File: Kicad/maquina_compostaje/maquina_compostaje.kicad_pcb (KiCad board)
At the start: 2 copper layers, 97 parts, among them J1 Conn_01x06, J2 Conn_01x09, J3 Conn_01x04, J4 Conn_01x04, J5 Conn_01x03, J6 Barrel_Jack_MountingPin, J7 Conn_01x06, J8 Conn_01x04, Q1 BC328, Q2 BC328, Q3 BC328, Q4 BC328, Q5 BC328, Q6 BC328, Q7 BC328, Q8 BC328, SW1 1825910-6, SW2 1825910-6, U1 ESP32-WROOM-32, U2 TLP281-4GB(F), U3 TLP281-4GB(F), U4 L298N, U5 L298N, U6 AMS1117-5.0, U7 AMS1117-3.3, U8 LM393, U9 A3144

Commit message: inicio del ruteo
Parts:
- added C17: 0.1uF, Capacitor_SMD:C_1206_3216Metric_Pad1.33x1.80mm_HandSolder, F.Cu at (96.4, 71.6)
- added C18: 10uF, Capacitor_SMD:C_1206_3216Metric_Pad1.33x1.80mm_HandSolder, F.Cu at (93.5, 71.6)
- added R33: 4.7K, Resistor_SMD:R_1206_3216Metric_Pad1.30x1.75mm_HandSolder, F.Cu at (120.4, 150.3)
- added R34: 4.7K, Resistor_SMD:R_1206_3216Metric_Pad1.30x1.75mm_HandSolder, F.Cu at (123.3, 150.2)
- added R35: 4.7K, Resistor_SMD:R_1206_3216Metric_Pad1.30x1.75mm_HandSolder, F.Cu at (92.1, 80.4)
- added R36: 4.7K, Resistor_SMD:R_1206_3216Metric_Pad1.30x1.75mm_HandSolder, F.Cu at (96.1, 76.5)
- D1, D10, D11, D12, D13, D14, D15, D16, D2, D3, D4, D5, D6, D7, D8, D9: footprint M7:DIOM505270X240 -> Diode_SMD:D_SOD-128
- D17: footprint Diode_THT:D_DO-41_SOD81_P10.16mm_Horizontal -> Diode_SMD:D_SOD-128
- J2: value Conn_01x09 -> Conenctor_GPIO; footprint Connector_JST:JST_EH_B9B-EH-A_1x09_P2.50mm_Vertical -> Connector_JST:JST_EH_B5B-EH-A_1x05_P2.50mm_Vertical
- Q1, Q2, Q3, Q4, Q5, Q6, Q7, Q8: footprint Package_TO_SOT_THT:TO-92_Inline -> Package_TO_SOT_SMD:SOT-23
- R2, R3: value 470 -> 4.7K
- SW1: value 1825910-6 -> RESET; footprint 1825910-6:SW_1825910-6-4 -> w_switch:smd_push2
- SW2: value 1825910-6 -> BOOT; footprint 1825910-6:SW_1825910-6-4 -> w_switch:smd_push2
- U2, U3: footprint TLP281-4GB_F_:SOIC127P700X210-16N -> Package_SO:SO-16_5.3x10.2mm_P1.27mm
- U6: footprint AMS1117-5:SOT229P700X180-4N -> Package_TO_SOT_SMD:SOT-223
- U7: footprint AMS1117-3:SOT229P700X180-4N -> Package_TO_SOT_SMD:SOT-223
- moved J8 94.7 mm to (153.6, 108.2), turned to 90 degrees
- moved J4 88.4 mm to (153.8, 137.1), turned to 90 degrees
- moved R20 78.7 mm to (72.4, 95.3), turned to -90 degrees
- moved R22 76.6 mm to (63.2, 110.5), turned to 90 degrees
- moved C3 71.3 mm to (84.3, 83.8)
- moved R23 69.0 mm to (70.6, 117.9), turned to 90 degrees
- moved R21 67.4 mm to (66.4, 114.7), turned to 90 degrees
- moved R25 67.3 mm to (83.9, 114.8), turned to 90 degrees
- moved C5 65.5 mm to (130.7, 98.5)
- moved R18 62.5 mm to (80.0, 95.3), turned to -90 degrees
- moved R19 61.3 mm to (76.2, 95.3), turned to -90 degrees
- moved Q7 60.7 mm to (76.5, 111.8), turned to 180 degrees
- moved Q6 59.0 mm to (71.6, 111.8), turned to 180 degrees
- moved J7 58.4 mm to (132.8, 152.4), turned to 0 degrees
- moved R28 56.8 mm to (88.2, 111.8), turned to 90 degrees
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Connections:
- net /ESP32/Hall_sensor renamed Hall_sensor
- net /ESP32/M_A1 renamed M_A1
- net /ESP32/M_A2 renamed M_A2
- net /ESP32/M_A3 renamed M_A3
- net /ESP32/M_A4 renamed M_A4
- net /ESP32/M_B1 renamed M_B1
- net /ESP32/M_B2 renamed M_B2
- net /ESP32/M_B3 renamed M_B3
- net /ESP32/M_B4 renamed M_B4
- net /ESP32/Touch_sensor renamed Touch_sensor
- net /Power supply/bypass 3.3v renamed 3.3V
- C10 pad 1: /Power supply/bypass 5v -> 5V
- C11 pad 1: /Power supply/bypass 5v -> 5V
- C12 pad 2: unconnected-(C12-Pad2) -> GND
- C3 pad 1: /Motor A/5V -> 5V
- C4 pad 1: /Motor A/12V -> 12V
- C5 pad 1: /Motor B/5V -> 5V
- C6 pad 1: /Motor A/12V -> 12V
- C8 pad 1: /Power supply/bypass 5v -> 5V
- C9 pad 1: /Power supply/bypass 5v -> 5V
- D18 pad 2: /Power supply/bypass 5v -> 5V
- D19 pad 2: /Power supply/bypass 5v -> 5V
- F2 pad 2: /Motor A/12V -> 12V
- J2 pad 2: /ESP32/gpio4 -> /ESP32/gpio16
- J2 pad 3: /ESP32/gpio5 -> /ESP32/gpio17
- J2 pad 4: /ESP32/gpio16 -> /ESP32/gpio23
- J2 pad 5: /ESP32/gpio17 -> /ESP32/gpio35
- J5 pad 1: /Power supply/bypass 5v -> 5V
- J7 pad 2: /ESP32/RX -> RX
- J7 pad 3: /ESP32/TX -> TX
- J7 pad 4: /Power supply/bypass 5v -> 5V
- J8 pad 1: /ESP32/SDA -> SDA
- J8 pad 2: /ESP32/SCL -> SCL
- Q5 pad 1: GND -> /Motor B/IN 4B
- Q6 pad 1: GND -> /Motor B/IN 3B
- Q7 pad 1: GND -> /Motor B/IN 2B
- R10 pad 1: /Motor A/12V -> 12V
- R11 pad 1: /Motor A/12V -> 12V
- R12 pad 1: /Motor A/12V -> 12V
- R13 pad 1: /Motor A/12V -> 12V
- R14 pad 1: /Motor A/12V -> 12V
- R15 pad 1: /Motor A/12V -> 12V
- R16 pad 1: /Motor A/12V -> 12V
- R2 pad 1: Net-(R2-Pad1) -> SCL
- R2 pad 2: /ESP32/RX -> +3.3V
- R21 pad 1: /Motor A/12V -> 12V
- R22 pad 1: /Motor A/12V -> 12V
- R22 pad 2: GND -> /Motor B/IN 4B
- R23 pad 1: /Motor A/12V -> 12V
- R24 pad 1: /Motor A/12V -> 12V
- R24 pad 2: GND -> /Motor B/IN 3B
- R25 pad 1: /Motor A/12V -> 12V
- R26 pad 1: /Motor A/12V -> 12V
- R26 pad 2: GND -> /Motor B/IN 2B
- R27 pad 1: /Motor A/12V -> 12V
- R28 pad 1: /Motor A/12V -> 12V
- R3 pad 1: Net-(R3-Pad1) -> SDA
- R3 pad 2: /ESP32/TX -> +3.3V
- R30 pad 1: /Power supply/bypass 5v -> 5V
- R32 pad 1: /Power supply/bypass 5v -> 5V
- R9 pad 1: /Motor A/12V -> 12V
- RV1 pad 1: +5V -> 5V
- U1 pad 26: /ESP32/gpio4 -> EN_1A
- U1 pad 29: /ESP32/gpio5 -> EN_2A
- U1 pad 33: /ESP32/SDA -> SDA
- U1 pad 34: Net-(R3-Pad1) -> TX
- U1 pad 35: Net-(R2-Pad1) -> RX
- U1 pad 36: /ESP32/SCL -> SCL
- U1 pad 6: /ESP32/gpio34 -> EN_2B
- U1 pad 9: /ESP32/gpio33 -> EN_1B
- U4 pad 11: /Motor A/EN B -> EN_2A
- U4 pad 4: /Motor A/12V -> 12V
- U4 pad 6: /Motor A/EN A -> EN_1A
- U4 pad 9: /Motor A/5V -> 5V
- U5 pad 10: GND -> /Motor B/IN 3B
- U5 pad 11: /Motor B/EN_2B -> EN_2B
- U5 pad 12: GND -> /Motor B/IN 4B
- U5 pad 4: /Motor A/12V -> 12V
- U5 pad 6: /Motor B/EN_1B -> EN_1B
- U5 pad 7: GND -> /Motor B/IN 2B
- U5 pad 9: /Motor B/5V -> 5V
- U6 pad 2: /Power supply/bypass 5v -> 5V
- U7 pad 3: /Power supply/bypass 5v -> 5V
- U8 pad 8: /Power supply/bypass 5v -> 5V
- U9 pad 1: /Power supply/bypass 5v -> 5V
- U9 pad 2: Net-(C16-Pad1) -> GND
- U9 pad 3: unconnected-(U9-Pad3) -> Net-(C16-Pad1)
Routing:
- net GND: track 0.00 -> 451.7 mm, vias 0 -> 12
- net 12V: track 0.00 -> 149.9 mm
- net 5V: track 0.00 -> 133.6 mm, vias 0 -> 2
- net /Motor B/IN 3B: track 0.00 -> 65.9 mm, vias 0 -> 1
- net /Motor A/IN 3A: track 0.00 -> 59.7 mm, vias 0 -> 1
- net /Motor B/IN 2B: track 0.00 -> 57.4 mm, vias 0 -> 1
- net /Motor B/IN 4B: track 0.00 -> 56.3 mm, vias 0 -> 1
- net /Motor A/IN 2A: track 0.00 -> 51.7 mm, vias 0 -> 1
- net 3.3V: track 0.00 -> 50.7 mm
- net /Motor A/IN 4A: track 0.00 -> 50.6 mm, vias 0 -> 1
- net /Motor B/OUT 1: track 0.00 -> 48.8 mm
- net /Motor A/OUT 1: track 0.00 -> 47.3 mm
- net /Motor B/IN 1B: track 0.00 -> 46.6 mm, vias 0 -> 2
- net /Motor A/IN 1A: track 0.00 -> 44.8 mm, vias 0 -> 2
- net /Motor B/OUT 4: track 0.00 -> 41.0 mm
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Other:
- board outline added: 99.9 x 99.9 mm

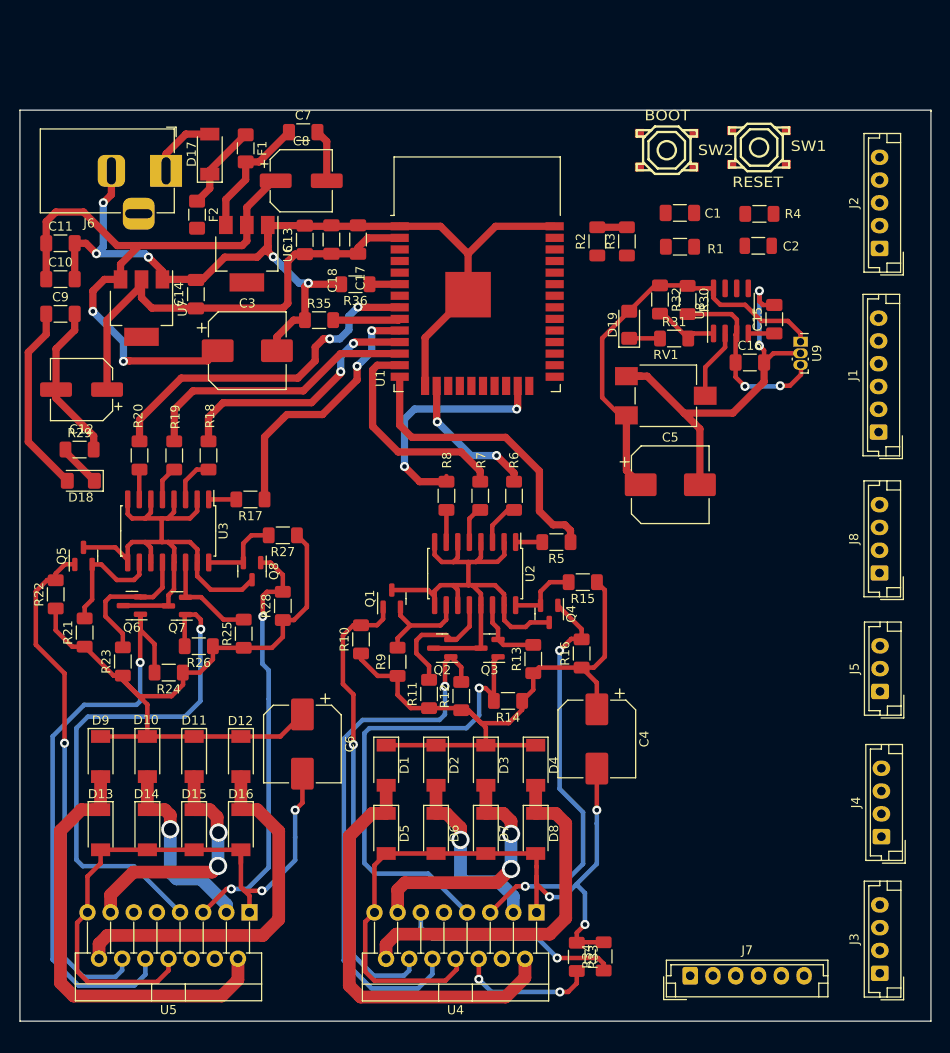
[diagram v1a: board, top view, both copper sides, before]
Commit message: se agregaron componentes en la parte inferior de la placa
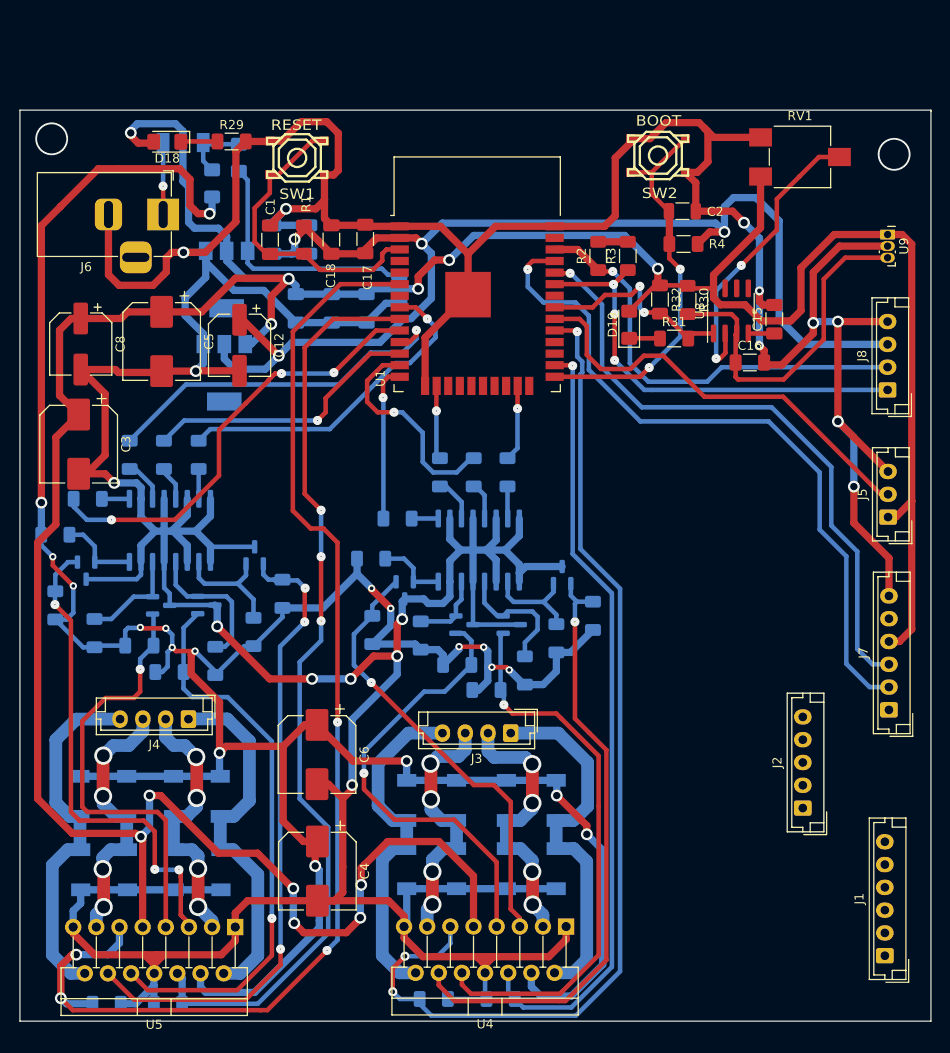
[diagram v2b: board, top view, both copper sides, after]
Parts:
- C10, C11, C13, C14, C7, C9, D1, D10, D11, D12, D13, D14, D15, D16, D17, D2, D3, D4, D5, D6, D7, D8, D9, F1, F2, Q1, Q2, Q3, Q4, Q5, Q6, Q7, Q8, R10, R11, R12, R13, R14, R15, R16, R17, R18, R19, R20, R21, R22, R23, R24, R25, R26, R27, R28, R33, R34, R35, R36, R5, R6, R7, R8, R9, U2, U3, U6, U7: moved to B.Cu
- J1: value Conn_01x06 -> OTHERS
- J2: value Conenctor_GPIO -> GPIO
- J5: value Conn_01x03 -> TOUCH_SENSOR
- J7: value Conn_01x06 -> SERIAL_USB
- J8: value Conn_01x04 -> OLED
- moved R36 83.5 mm to (68.8, 155.4), turned to 0 degrees
- moved J4 77.1 mm to (77.8, 124.2), turned to 180 degrees
- moved R35 76.8 mm to (75.6, 155.4)
- moved J2 62.0 mm to (145.2, 134.0)
- moved C5 58.0 mm to (74.8, 82.8), turned to -90 degrees
- moved J1 57.5 mm to (154.2, 150.2)
- moved SW1 50.7 mm to (89.7, 62.6)
- moved J3 48.3 mm to (113.2, 125.8), turned to 180 degrees
- moved C1 45.1 mm to (86.8, 71.6), turned to 90 degrees
- moved R1 41.3 mm to (90.5, 71.6), turned to -90 degrees
- moved D18 38.4 mm to (75.5, 60.9)
- moved R29 37.7 mm to (82.5, 60.8)
- moved J7 36.4 mm to (154.7, 123.2), turned to 90 degrees
- moved C4 33.9 mm to (91.9, 140.9)
- moved C9 33.6 mm to (97.3, 79.2), turned to -90 degrees
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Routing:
- net 5V: track 133.6 -> 366.6 mm, vias 2 -> 12
- net GND: track 451.7 -> 669.9 mm, vias 12 -> 17
- net 12V: track 149.9 -> 321.4 mm, vias 0 -> 19
- net EN_2B: track 3.31 -> 134.2 mm, vias 0 -> 4
- net EN_1B: track 7.35 -> 101.9 mm, vias 0 -> 3
- net EN_2A: track 24.2 -> 115.1 mm, vias 1 -> 3
- net 3.3V: track 50.7 -> 136.4 mm, vias 0 -> 4
- net RX: track 0.00 -> 77.4 mm, vias 0 -> 1
- net EN_1A: track 15.3 -> 85.8 mm, vias 2 -> 1
- net TX: track 0.00 -> 68.6 mm, vias 0 -> 1
- net SDA: track 0.00 -> 50.4 mm, vias 0 -> 3
- net SCL: track 0.00 -> 48.1 mm, vias 0 -> 1
- net Touch_sensor: track 0.00 -> 47.6 mm
- net Net-(C2-Pad1): track 0.00 -> 42.4 mm, vias 0 -> 2
- net Net-(C1-Pad1): track 0.00 -> 34.2 mm
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
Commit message: PCB ACTUALIZADA
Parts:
- moved J2 11.5 mm to (154.7, 140.5)
- moved J1 7.64 mm to (147.1, 152.9), turned to 180 degrees
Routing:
- net /ESP32/gpio23: track 0.00 -> 100.0 mm, vias 0 -> 2
- net /ESP32/gpio35: track 0.00 -> 94.9 mm, vias 0 -> 2
- net /ESP32/SCS: track 0.00 -> 89.4 mm, vias 0 -> 2
- net /ESP32/SD3: track 0.00 -> 88.3 mm, vias 0 -> 2
- net /ESP32/SCK: track 0.00 -> 86.5 mm, vias 0 -> 2
- net /ESP32/SD2: track 0.00 -> 85.8 mm, vias 0 -> 2
- net /ESP32/SD1: track 0.00 -> 84.9 mm
- net /ESP32/gpio16: track 0.00 -> 84.7 mm, vias 0 -> 2
- net /ESP32/gpio17: track 0.00 -> 84.4 mm, vias 0 -> 2
- net /ESP32/SD0: track 0.00 -> 82.1 mm
- net /ESP32/gpio2: track 0.00 -> 81.4 mm
